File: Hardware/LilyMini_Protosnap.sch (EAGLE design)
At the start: 69 parts, among them Q1 ZXMP6A13F, U1 SAMD11D14A-M, U2 AP2112K-3.3V, U3 ALS-PT19, Y1 32.768kHz

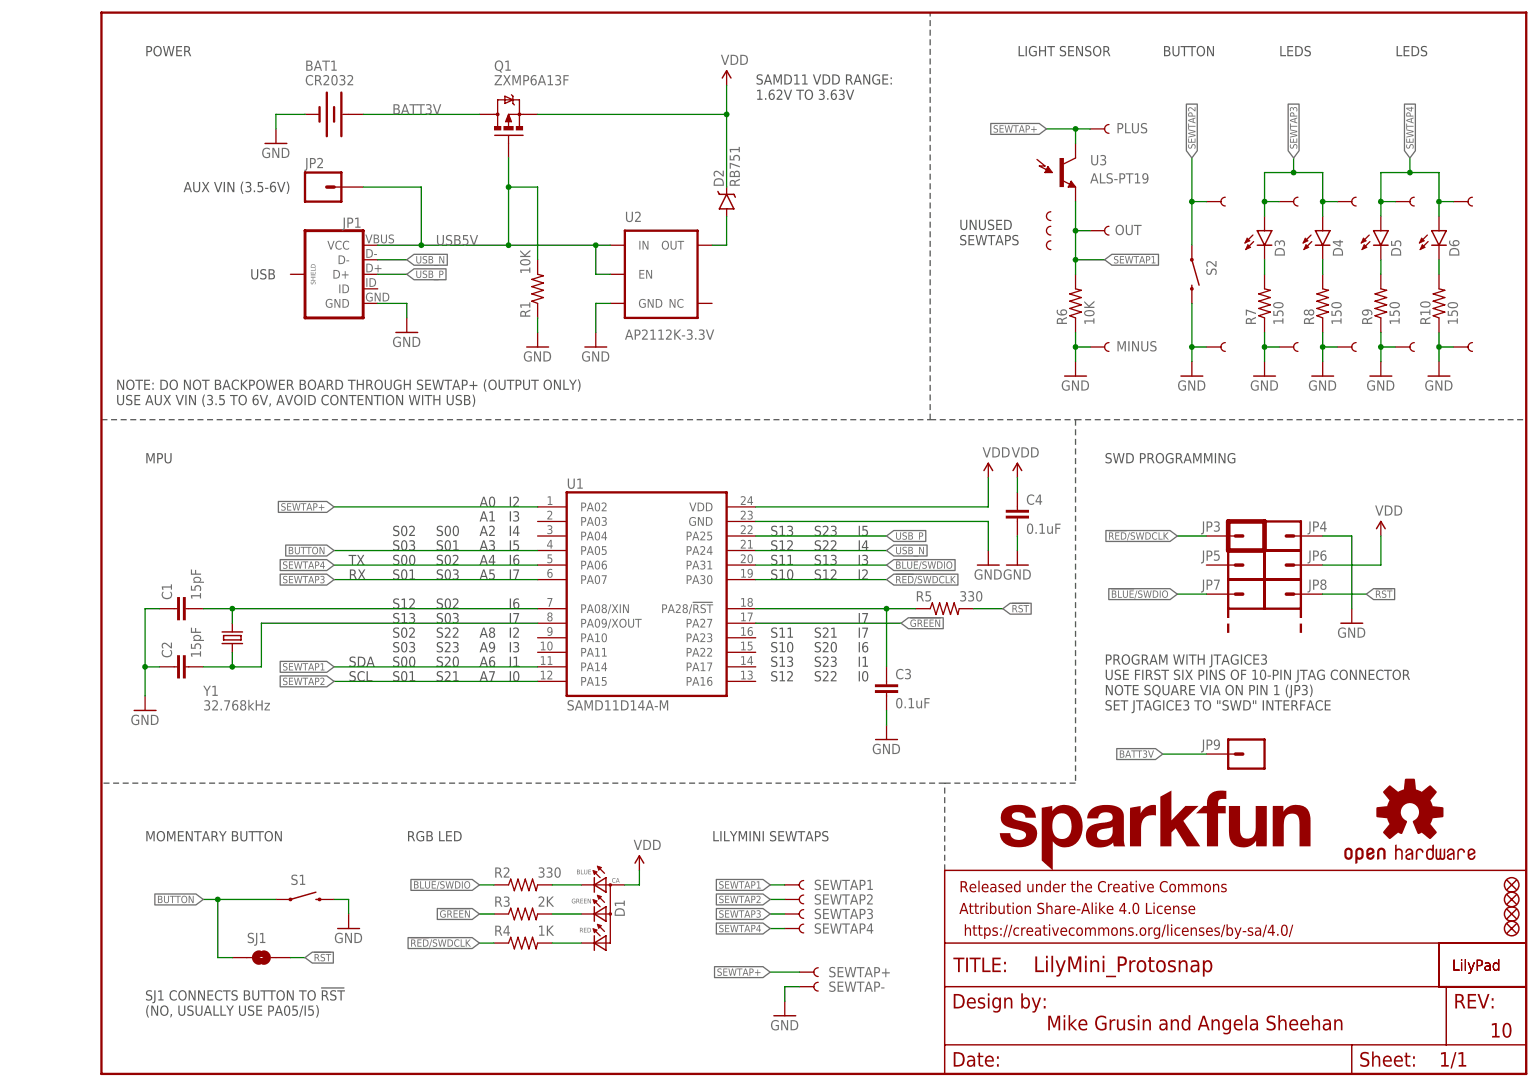
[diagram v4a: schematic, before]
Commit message: Fixed typo on schematic
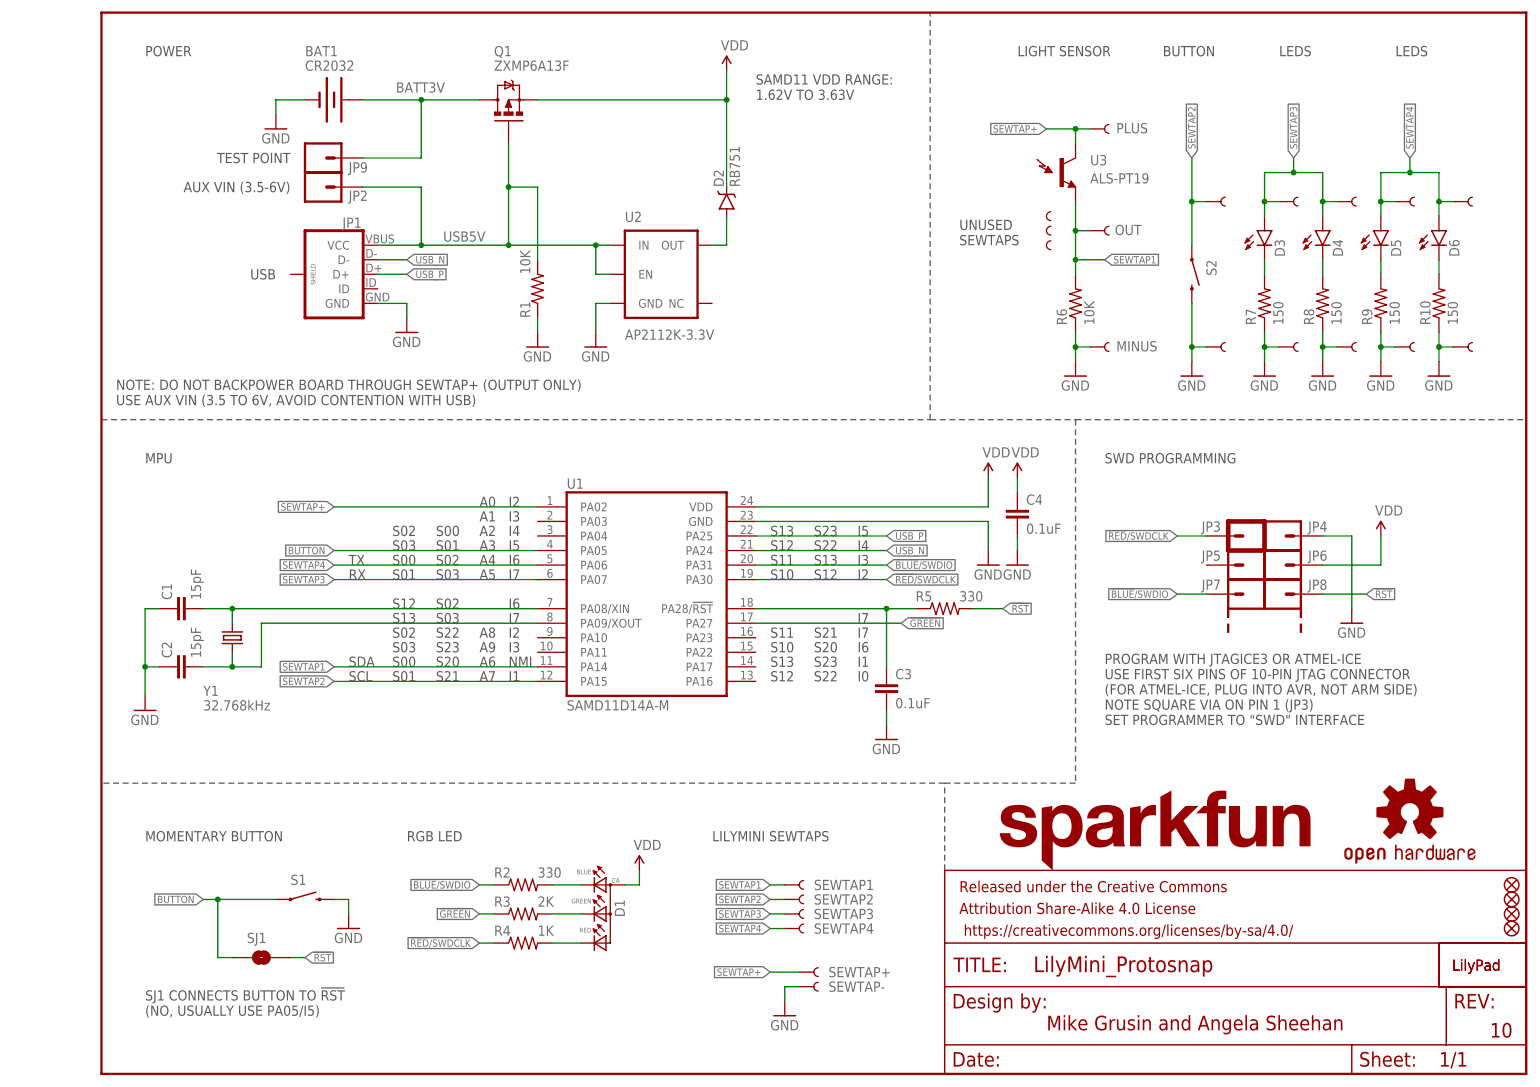
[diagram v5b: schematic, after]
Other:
- note added: "NMI"
- note added: "PROGRAM WITH JTAGICE3 OR ATMEL-ICE USE FIRST SIX PINS OF 10-PIN JTAG CONNECTOR (FOR ATMEL-ICE, PLUG INTO AVR, NOT ARM SIDE) NOTE SQUARE VIA ON PIN 1 (JP3) SET PROGRAMMER TO "SWD" INTERFACE"
- note added: "TEST POINT"
- note removed: "PROGRAM WITH JTAGICE3 USE FIRST SIX PINS OF 10-PIN JTAG CONNECTOR NOTE SQUARE VIA ON PIN 1 (JP3) SET JTAGICE3 TO "SWD" INTERFACE"
- moved on the sheet: BAT1, JP9, Q1
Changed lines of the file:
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@@
 <sheet>
 <plain>
-<text x="175.26" y="63.5" size="1.778" layer="97">PROGRAM WITH JTAGICE3
+<text x="175.26" y="60.96" size="1.778" layer="97">PROGRAM WITH JTAGICE3 OR ATMEL-ICE
 USE FIRST SIX PINS OF 10-PIN JTAG CONNECTOR
+(FOR ATMEL-ICE, PLUG INTO AVR, NOT ARM SIDE)
 NOTE SQUARE VIA ON PIN 1 (JP3)
-SET JTAGICE3 TO "SWD" INTERFACE</text>
+SET PROGRAMMER TO "SWD" INTERFACE</text>
 <text x="114.3" y="170.18" size="1.778" layer="97">SAMD11 VDD RANGE:
 1.62V TO 3.63V</text>
@@
 <text x="71.12" y="76.2" size="1.778" layer="97">I2</text>
 <text x="71.12" y="73.66" size="1.778" layer="97">I3</text>
-<text x="71.12" y="71.12" size="1.778" layer="97">I1</text>
-<text x="71.12" y="68.58" size="1.778" layer="97">I0</text>
+<text x="71.12" y="71.12" size="1.778" layer="97">NMI</text>
+<text x="71.12" y="68.58" size="1.778" layer="97">I1</text>
 <text x="132.08" y="93.98" size="1.778" layer="97">I5</text>
 <text x="116.84" y="93.98" size="1.778" layer="97">S13</text>
@@
 <text x="7.62" y="10.16" size="1.778" layer="97">SJ1 CONNECTS BUTTON TO !RST!
 (NO, USUALLY USE PA05/I5)</text>
+<text x="33.02" y="160.02" size="1.778" layer="97" rot="R180" align="center-left">TEST POINT</text>
 </plain>
 <instances>
@@
 <instance part="GND4" gate="1" x="53.34" y="129.54"/>
 <instance part="SUPPLY3" gate="VDD" x="154.94" y="104.14"/>
-<instance part="BAT1" gate="G$1" x="40.64" y="167.64" smashed="yes" rot="R180">
-<attribute name="NAME" x="35.56" y="175.26" size="1.778" layer="95"/>
-<attribute name="VALUE" x="35.56" y="172.72" size="1.778" layer="96"/>
-</instance>
-<instance part="GND2" gate="1" x="30.48" y="162.56"/>
+<instance part="BAT1" gate="G$1" x="40.64" y="170.18" smashed="yes" rot="R180">
+<attribute name="NAME" x="35.56" y="177.8" size="1.778" layer="95"/>
+<attribute name="VALUE" x="35.56" y="175.26" size="1.778" layer="96"/>
+</instance>
+<instance part="GND2" gate="1" x="30.48" y="165.1"/>
 <instance part="SEWTAP+" gate="G$1" x="124.46" y="17.78" smashed="yes">
 <attribute name="NAME" x="127" y="17.78" size="1.778" layer="95" align="center-left"/>
@@
 </instance>
 <instance part="GND5" gate="1" x="76.2" y="127"/>
-<instance part="Q1" gate="G$1" x="71.12" y="167.64" smashed="yes" rot="R90">
-<attribute name="NAME" x="68.58" y="175.26" size="1.778" layer="95"/>
-<attribute name="VALUE" x="68.58" y="172.72" size="1.778" layer="96"/>
+<instance part="Q1" gate="G$1" x="71.12" y="170.18" smashed="yes" rot="R90">
+<attribute name="NAME" x="68.58" y="177.8" size="1.778" layer="95"/>
+<attribute name="VALUE" x="68.58" y="175.26" size="1.778" layer="96"/>
 </instance>
 <instance part="D2" gate="G$1" x="109.22" y="152.4" rot="R90"/>
 <instance part="U2" gate="G$1" x="99.06" y="139.7"/>
 <instance part="GND6" gate="1" x="86.36" y="127"/>
-<instance part="SUPPLY2" gate="VDD" x="109.22" y="172.72"/>
+<instance part="SUPPLY2" gate="VDD" x="109.22" y="175.26"/>
 <instance part="GND7" gate="1" x="119.38" y="10.16"/>
-<instance part="JP2" gate="G$1" x="38.1" y="154.94"/>
+<instance part="JP2" gate="G$1" x="38.1" y="154.94" smashed="yes">
+<attribute name="VALUE" x="35.56" y="149.86" size="1.778" layer="96"/>
+<attribute name="NAME" x="43.18" y="152.527" size="1.778" layer="95"/>
+</instance>
 <instance part="Y1" gate="G$1" x="22.86" y="76.2" smashed="yes" rot="R90">
 <attribute name="NAME" x="17.78" y="66.04" size="1.778" layer="95"/>
@@
 <instance part="FD4" gate="G$1" x="246.38" y="30.48"/>
 <instance part="LOGO4" gate="G$1" x="154.94" y="35.56"/>
-<instance part="JP9" gate="G$1" x="200.66" y="55.88" smashed="yes" rot="R180">
-<attribute name="VALUE" x="203.2" y="60.96" size="1.778" layer="96" rot="R180"/>
-<attribute name="NAME" x="195.58" y="56.642" size="1.778" layer="95" rot="MR0"/>
+<instance part="JP9" gate="G$1" x="38.1" y="160.02" smashed="yes">
+<attribute name="VALUE" x="35.56" y="154.94" size="1.778" layer="96"/>
+<attribute name="NAME" x="43.18" y="159.258" size="1.778" layer="95" rot="MR180"/>
 </instance>
 <instance part="SJ1" gate="G$1" x="27.94" y="20.32"/>
@@
 <wire x1="71.12" y1="144.78" x2="86.36" y2="144.78" width="0.1524" layer="91"/>
 <wire x1="86.36" y1="144.78" x2="88.9" y2="144.78" width="0.1524" layer="91"/>
-<wire x1="71.12" y1="160.02" x2="71.12" y2="154.94" width="0.1524" layer="91"/>
+<wire x1="71.12" y1="162.56" x2="71.12" y2="154.94" width="0.1524" layer="91"/>
 <junction x="71.12" y="144.78"/>
 <wire x1="71.12" y1="154.94" x2="71.12" y2="144.78" width="0.1524" layer="91"/>
@@
 <junction x="86.36" y="144.78"/>
 <wire x1="48.26" y1="144.78" x2="55.88" y2="144.78" width="0.1524" layer="91"/>
-<label x="58.42" y="144.78" size="1.778" layer="95"/>
+<label x="59.69" y="145.415" size="1.778" layer="95"/>
 <pinref part="JP2" gate="G$1" pin="1"/>
 <wire x1="55.88" y1="144.78" x2="71.12" y2="144.78" width="0.1524" layer="91"/>
@@
 <pinref part="BAT1" gate="G$1" pin="-"/>
 <pinref part="GND2" gate="1" pin="GND"/>
-<wire x1="30.48" y1="165.1" x2="30.48" y2="167.64" width="0.1524" layer="91"/>
-<wire x1="30.48" y1="167.64" x2="35.56" y2="167.64" width="0.1524" layer="91"/>
+<wire x1="30.48" y1="167.64" x2="30.48" y2="170.18" width="0.1524" layer="91"/>
+<wire x1="30.48" y1="170.18" x2="35.56" y2="170.18" width="0.1524" layer="91"/>
 </segment>
 <segment>
@@
 <segment>
 <pinref part="Q1" gate="G$1" pin="S"/>
-<wire x1="76.2" y1="167.64" x2="109.22" y2="167.64" width="0.1524" layer="91"/>
-<junction x="109.22" y="167.64"/>
-<wire x1="109.22" y1="154.94" x2="109.22" y2="167.64" width="0.1524" layer="91"/>
+<wire x1="76.2" y1="170.18" x2="109.22" y2="170.18" width="0.1524" layer="91"/>
+<junction x="109.22" y="170.18"/>
+<wire x1="109.22" y1="154.94" x2="109.22" y2="170.18" width="0.1524" layer="91"/>
 <pinref part="D2" gate="G$1" pin="C"/>
 <pinref part="SUPPLY2" gate="VDD" pin="VDD"/>
-<wire x1="109.22" y1="167.64" x2="109.22" y2="172.72" width="0.1524" layer="91"/>
+<wire x1="109.22" y1="170.18" x2="109.22" y2="175.26" width="0.1524" layer="91"/>
 </segment>
 </net>
@@
 <net name="BATT3V" class="0">
 <segment>
+<pinref part="JP9" gate="G$1" pin="1"/>
+<wire x1="45.72" y1="160.02" x2="55.88" y2="160.02" width="0.1524" layer="91"/>
 <pinref part="BAT1" gate="G$1" pin="+"/>
 <pinref part="Q1" gate="G$1" pin="D"/>
-<label x="50.8" y="167.64" size="1.778" layer="95"/>
-<wire x1="45.72" y1="167.64" x2="66.04" y2="167.64" width="0.1524" layer="91"/>
-</segment>
-<segment>
-<pinref part="JP9" gate="G$1" pin="1"/>
-<wire x1="193.04" y1="55.88" x2="185.42" y2="55.88" width="0.1524" layer="91"/>
-<label x="185.42" y="55.88" size="1.27" layer="95" rot="R180" xref="yes"/>
-</segment>
-</net>
+<label x="51.435" y="171.45" size="1.778" layer="95"/>
+<wire x1="45.72" y1="170.18" x2="55.88" y2="170.18" width="0.1524" layer="91"/>
+<wire x1="55.88" y1="170.18" x2="66.04" y2="170.18" width="0.1524" layer="91"/>
+<wire x1="55.88" y1="160.02" x2="55.88" y2="170.18" width="0.1524" layer="91"/>
+<junction x="55.88" y="170.18"/>
+</segment>
+</net>
